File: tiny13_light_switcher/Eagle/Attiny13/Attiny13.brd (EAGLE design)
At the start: 63 x 83 mm, 39 parts, among them Q4 2N7000, Q5 2N7000, Q6 2N7000, U1 ATTiny13, U2 ATTiny85

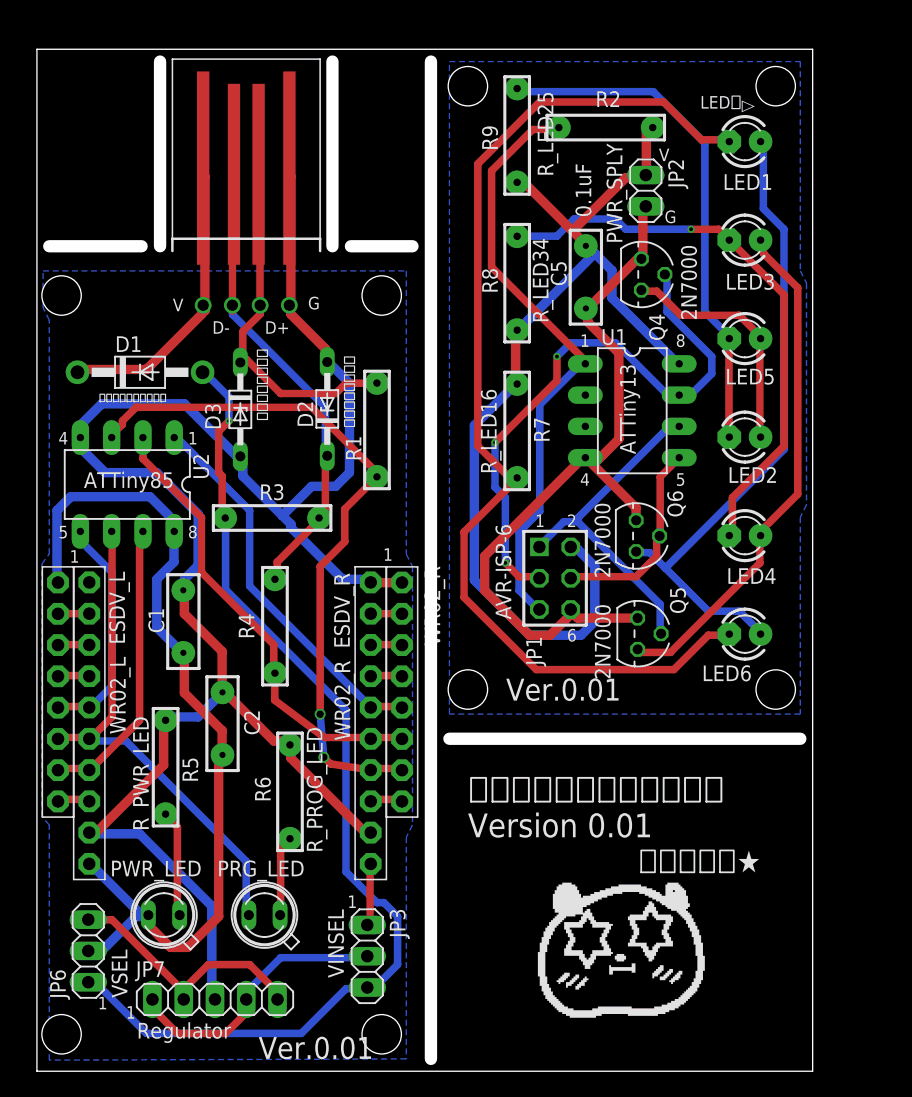
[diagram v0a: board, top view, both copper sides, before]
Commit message: Change PCB Size.
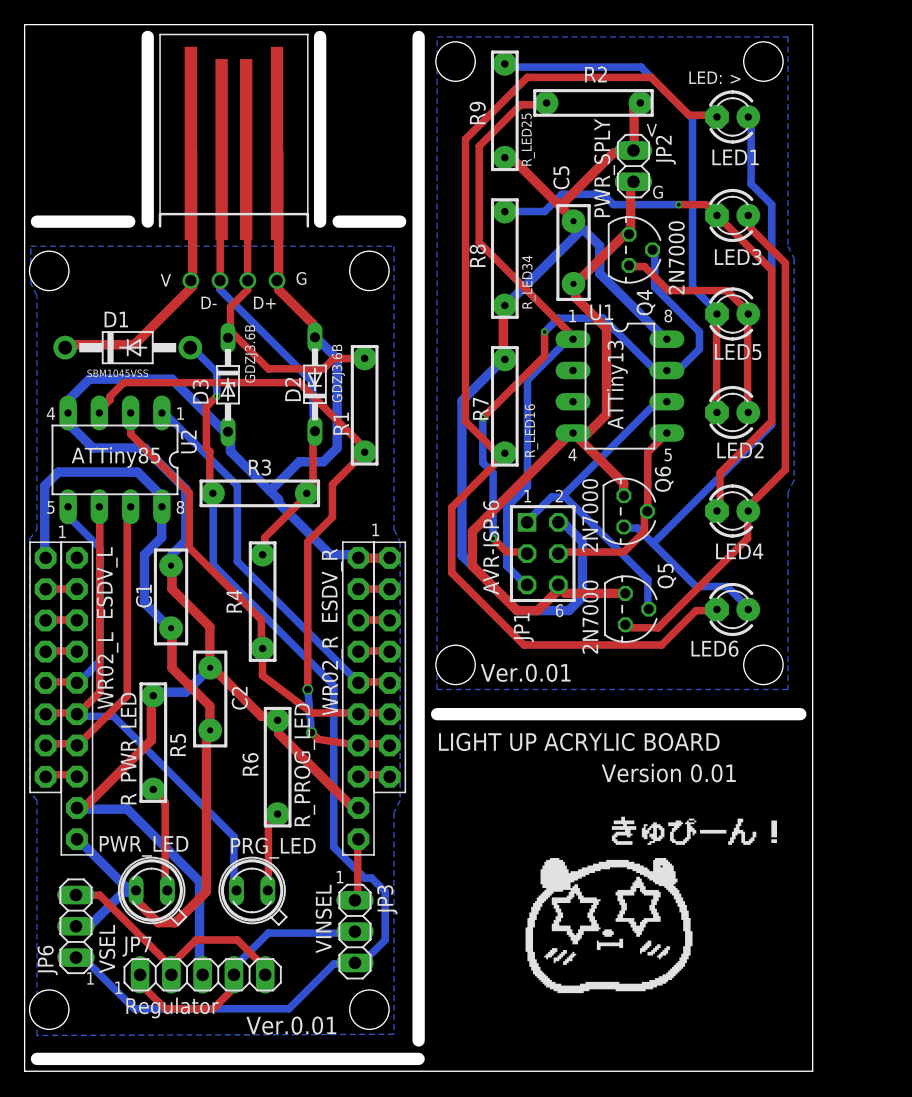
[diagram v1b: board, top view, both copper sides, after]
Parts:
- D1: value ＳＢＭ１０４５ＶＳＳ -> SBM1045VSS
- D2, D3: value ＧＤＺＪ３．６Ｂ -> GDZJ3.6B
- moved C1 2.24 mm to (11.9, 38.5)
- moved C2 2.24 mm to (15.1, 30.2)
- moved C5 2.24 mm to (44.6, 66.5)
- moved D1 2.24 mm to (8.37, 58.8)
- moved D2 2.24 mm to (23.6, 55.8)
- moved D3 2.24 mm to (16.5, 55.8)
- moved ESDV_L 2.24 mm to (4.25, 30.3)
- moved ESDV_R 2.24 mm to (27.1, 30.3)
- moved JP1 2.24 mm to (42.1, 42.0)
- moved JP2 2.24 mm to (49.5, 73.5)
- moved JP3 2.24 mm to (26.8, 11.3)
- moved JP6 2.24 mm to (4.17, 11.8)
- moved JP7 2.24 mm to (14.5, 7.83)
- moved LED1 2.24 mm to (57.5, 77.5)
- moved LED2 2.24 mm to (57.5, 53.5)
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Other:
- board size 63 x 83 mm -> 64 x 85 mm
- board text added: ">"
- board text added: "LED:"
- board text added: "LIGHT UP ACRYLIC BOARD"
- board text added: "Version 0.01"
- board text removed: "LED："
- board text removed: "▽"
- board text removed: "アクリルライトアップ基板 Version 0.01"
- board text removed: "キュピーン★"

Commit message: Fix LED Direction & USB SMD Length.
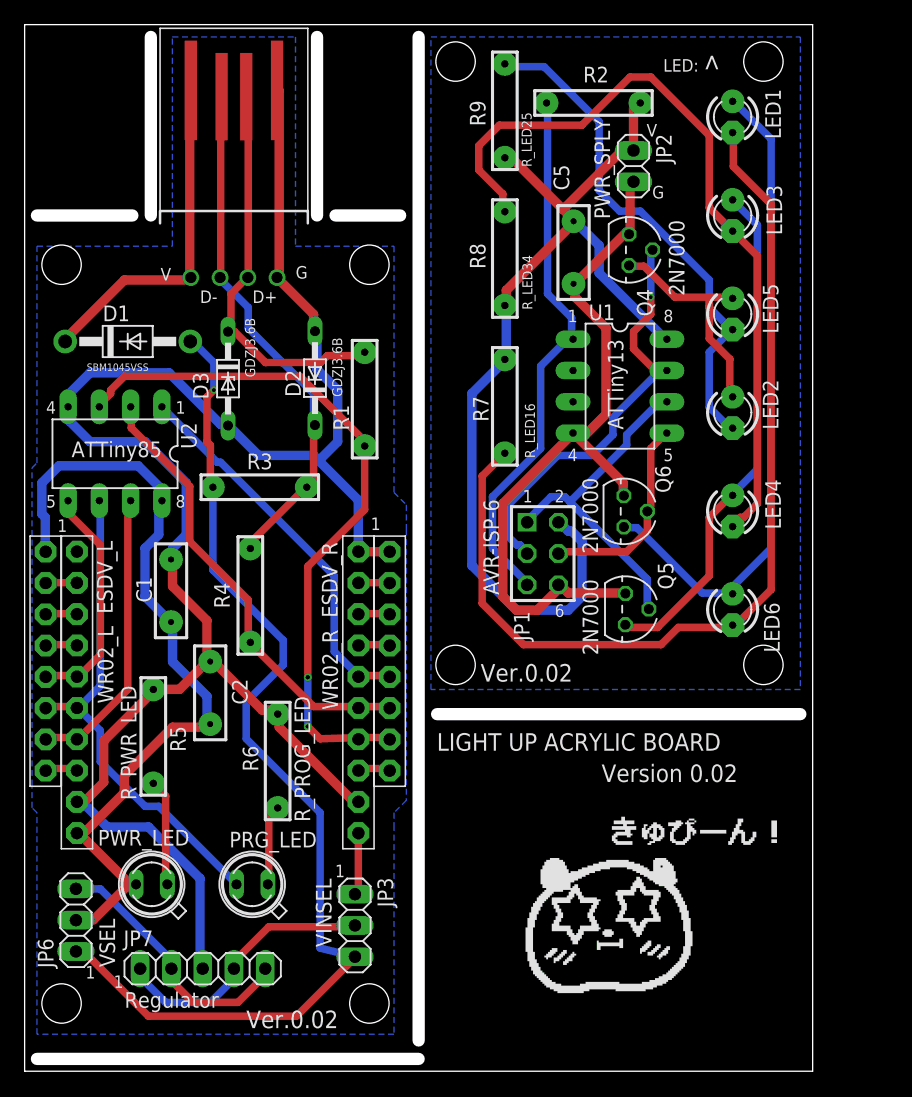
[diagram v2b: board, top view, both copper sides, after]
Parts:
- moved R4 1.12 mm to (18.3, 38.6)
- moved C1 0.50 mm to (11.9, 39.0)
- moved C2 0.50 mm to (15.1, 30.7)
- moved D1 0.50 mm to (8.37, 59.3)
- moved D2 0.50 mm to (23.6, 56.3)
- moved D3 0.50 mm to (16.5, 56.2)
- moved ESDV_L 0.50 mm to (4.25, 30.8)
- moved ESDV_R 0.50 mm to (27.1, 30.8)
- moved JP3 0.50 mm to (26.8, 11.8)
- moved JP6 0.50 mm to (4.17, 12.3)
- moved JP7 0.50 mm to (14.5, 8.33)
- moved LED8 0.50 mm to (18.5, 15.2)
- moved LED9 0.50 mm to (10.3, 15.2)
- moved R1 0.50 mm to (27.6, 54.6)
- moved R3 0.50 mm to (19.1, 47.4)
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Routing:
- net N$31: track 46.3 -> 63.7 mm, vias 1 -> 0
- net N$2: track 47.6 -> 35.2 mm, vias 3 -> 1
- net N$30: track 87.9 -> 78.3 mm
- net +5V: track 72.1 -> 66.2 mm
- net N$7: track 49.2 -> 44.2 mm
- net N$4: track 39.0 -> 42.2 mm
- net N$19: track 29.5 -> 32.5 mm
- net N$1: track 25.0 -> 27.8 mm
- net GND: track 62.5 -> 60.2 mm
- net VDD: track 85.0 -> 86.9 mm
- net VCC: track 83.5 -> 81.7 mm
- net N$5: track 52.4 -> 53.9 mm
- net N$9: track 19.4 -> 18.4 mm
- net N$11: track 56.9 -> 57.9 mm
- net N$15: track 41.6 -> 40.7 mm
- added copper zone on layer 16, net N$33
- added copper zone on layer 16, net N$34
- removed copper zone on layer 16, net AGND
- removed copper zone on layer 16, net GND
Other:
- outline, holes or cut-outs redrawn
- board text added: "Ver.0.02"
- board text added: "Version 0.02"
- board text removed: "Ver.0.01"
- board text removed: "Version 0.01"

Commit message: Spread Pin holes & Change LED Direction.
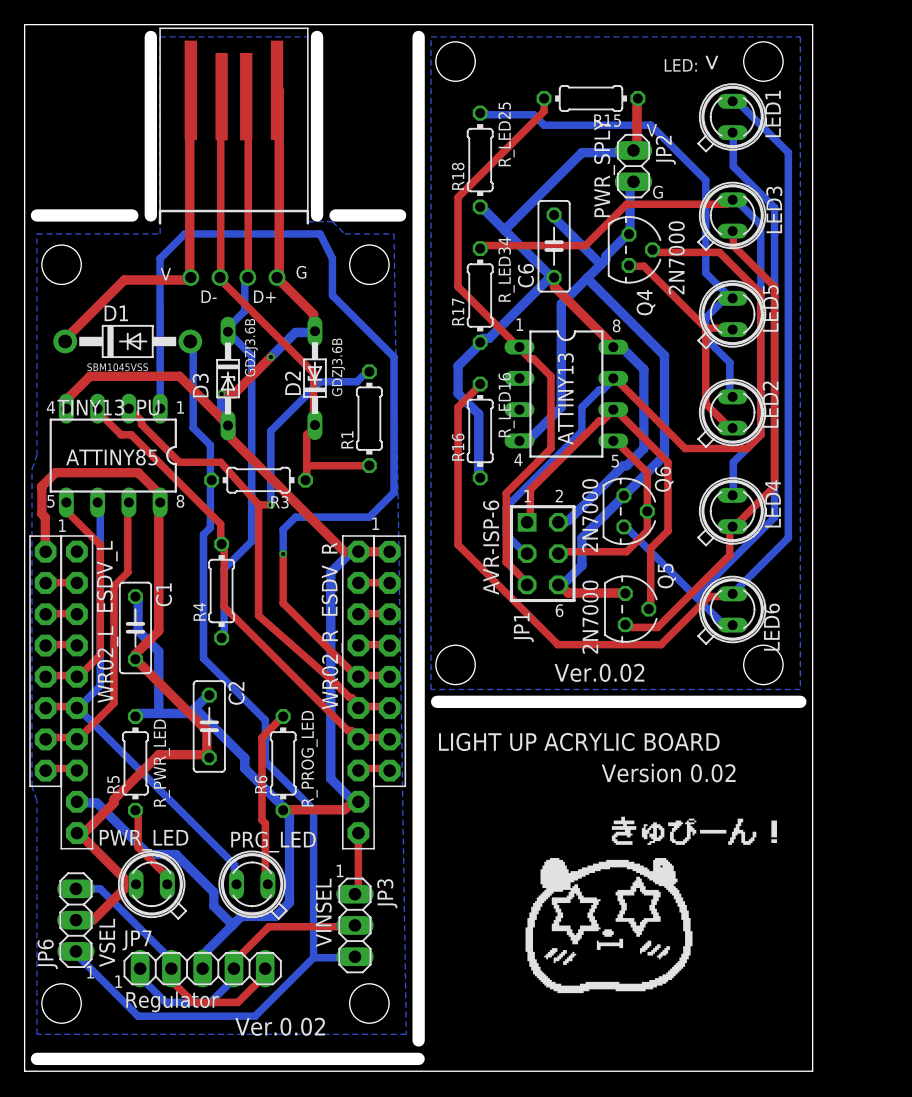
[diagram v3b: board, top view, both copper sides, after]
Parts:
- removed C5: 0.1uF, MyLib:CAP_DIP_2
- removed R2: 4K7, MyLib:R_0.125W_3
- removed R7: R_LED16, MyLib:R_0.125W_3
- removed R8: R_LED34, MyLib:R_0.125W_3
- removed R9: R_LED25, MyLib:R_0.125W_3
- removed U1: ATTiny13, atmel:DIL08
- removed U2: ATTiny85, atmel:DIL08
- added ATTINY13, ATTINY85: TINY13_PU, MyParts:TINY_DIL08
- added C6: 0.1uF, resistor:C050-025X075
- added R15: 4K7, resistor:0204/7
- added R16: R_LED16, resistor:0204/7
- added R17: R_LED34, resistor:0204/7
- added R18: R_LED25, resistor:0204/7
- C1, C2: device MyLib:CAP_DIP_2 -> resistor:C050-025X075
- LED1, LED2, LED3, LED4, LED5, LED6: device led:LED3MM -> led:SFH480
- R1, R3, R4, R5, R6: device MyLib:R_0.125W_3 -> resistor:0204/7
- moved C1 4.18 mm to (9.00, 36.0), turned to 90 degrees
- moved C2 2.73 mm to (15.0, 28.0), turned to 90 degrees
- moved R5 2.63 mm to (9.00, 25.0), turned to 90 degrees
- moved R4 2.36 mm to (16.0, 39.0)
- moved R1 1.63 mm to (28.0, 53.0)
- moved R3 0.58 mm to (19.0, 48.0)
- moved R6 0.49 mm to (21.0, 25.0)
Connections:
- net +5V: now also ATTINY85.8, C1.1, C2.1; no longer C1.2, C2.2, U2.8
- net AGND: now also ATTINY85.4, C1.2, C2.2, R5.2, R6.1; no longer C1.1, C2.1, R5.1, R6.2, U2.4
- net GND: now also ATTINY13.4, C6.2; no longer C5.1, U1.4
- net N$11: now also ATTINY85.3, R4.2; no longer R1.1, U2.3
- net N$12: now also ATTINY85.1; no longer U2.1
- net N$13: now also R5.1; no longer R5.2
- net N$14: now also R6.2; no longer R6.1
- net N$15: now also ATTINY85.6; no longer U2.6
- net N$16: now also ATTINY85.5; no longer U2.5
- net N$18: now also ATTINY85.7; no longer U2.7
- net N$19: now also R4.1; no longer R1.2
- net N$2: now also ATTINY13.7; no longer U1.7
- net N$3: now also ATTINY85.2, R1.2; no longer R4.1, U2.2
- net N$30: now also R16.2; no longer R7.2
- net N$31: now also R17.2; no longer R8.2
- net N$32: now also R18.2; no longer R9.2
- net N$4: now also R1.1; no longer R4.2
- net N$6: now also ATTINY13.5; no longer U1.5
- net N$7: now also ATTINY13.1, R15.2; no longer R2.1, U1.1
- net N$8: now also ATTINY13.6; no longer U1.6
- net VCC: now also ATTINY13.8, C6.1, R15.1, R16.1, R17.1, R18.1; no longer C5.2, R2.2, R7.1, R8.1, R9.1, U1.8
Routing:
- net N$12: track 31.3 -> 77.1 mm, vias 0 -> 1
- net N$2: track 35.2 -> 55.5 mm, vias 1 -> 0
- net N$11: track 57.9 -> 39.1 mm, vias 2 -> 0
- net N$3: track 36.9 -> 54.6 mm, vias 0 -> 1
- net N$31: track 63.7 -> 48.4 mm
- net N$19: track 32.5 -> 46.7 mm
- net VCC: track 81.7 -> 73.1 mm
- net N$14: track 6.52 -> 14.5 mm
- net GND: track 60.2 -> 68.1 mm
- net AGND: track 153.6 -> 160.8 mm, vias 0 -> 2
- net N$30: track 78.3 -> 85.2 mm
- net VDD: track 86.9 -> 81.8 mm, vias 1 -> 0
- net N$7: track 44.2 -> 47.9 mm
- net N$8: track 27.7 -> 31.0 mm
- net N$4: track 42.2 -> 39.8 mm
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- added copper zone on layer 16, net AGND
- added copper zone on layer 16, net GND
- removed copper zone on layer 16, net N$33
- removed copper zone on layer 16, net N$34
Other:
- outline, holes or cut-outs redrawn
- board text added: "<"
- board text removed: ">"
